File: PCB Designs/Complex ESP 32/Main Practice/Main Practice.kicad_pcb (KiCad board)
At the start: 4 copper layers, 87 parts, among them J1 SS-52400-002, J2 B2B-PH-SM4-TB, J3 GSD090012SEU, J5 Conn_01x04_Pin, J6 Conn_01x05_Pin, Q1 TEMT6000X01, Q2 BC817, Q3 BC817, U1 MCP73871, U2 BME280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

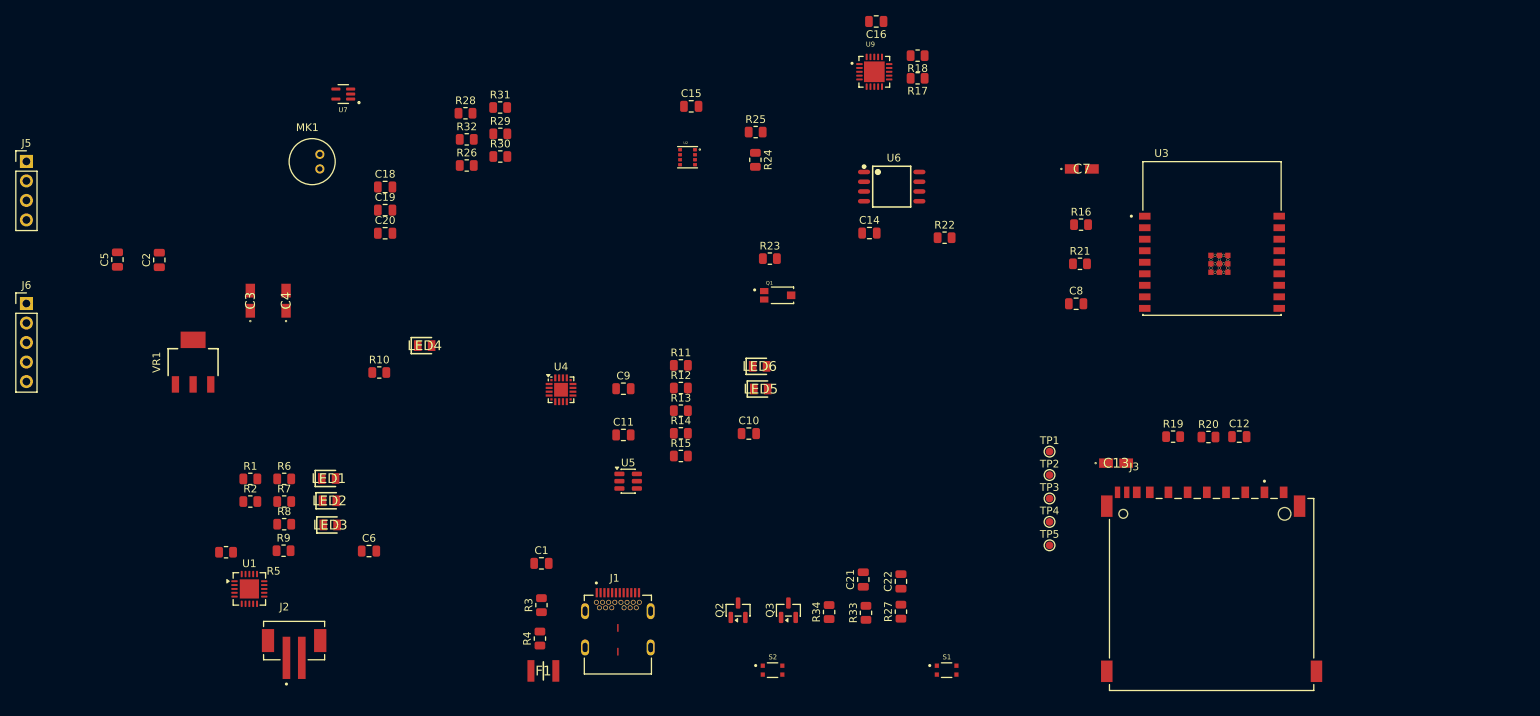
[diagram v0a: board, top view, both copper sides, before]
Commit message: reordered components around for optimal wiring
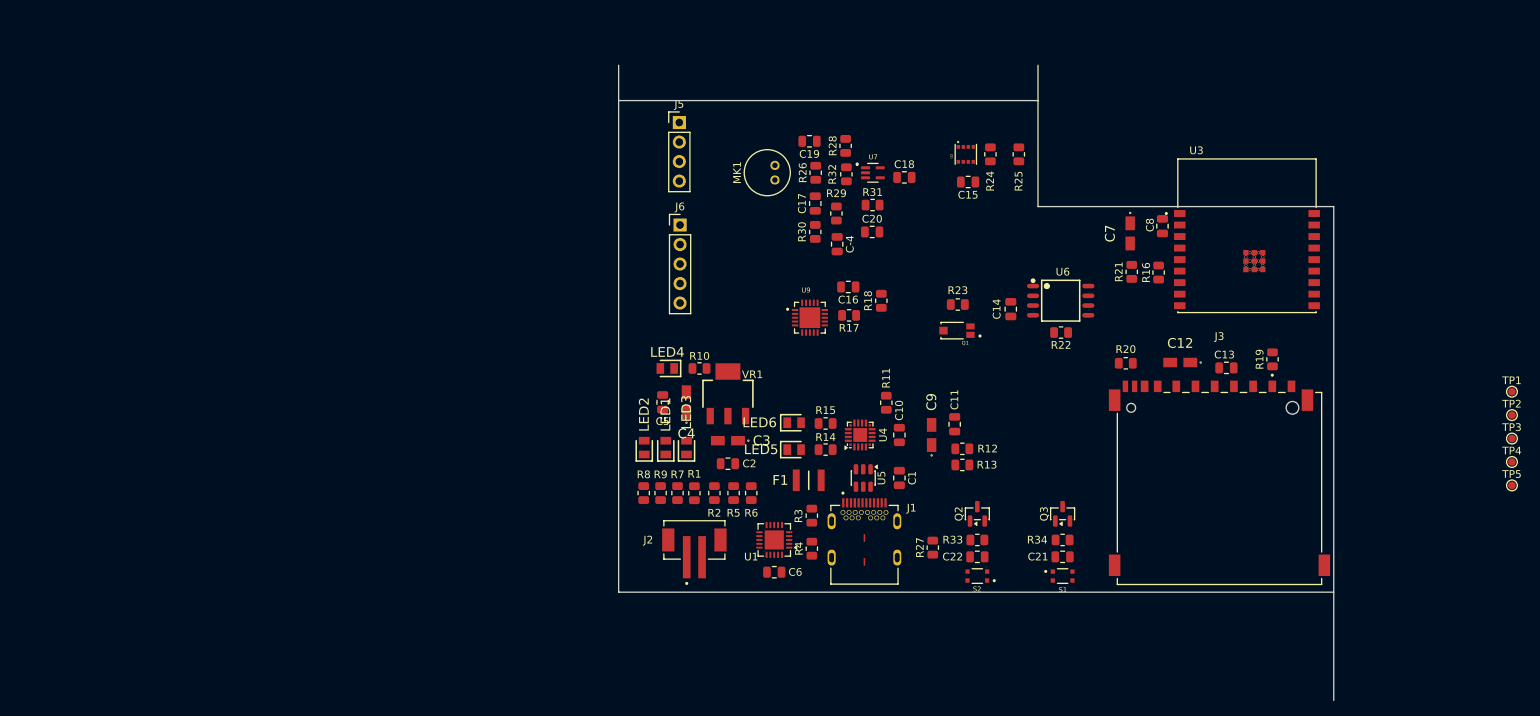
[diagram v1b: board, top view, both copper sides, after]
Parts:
- added C-4: 1u, Capacitor_SMD:C_0805_2012Metric, F.Cu at (179.6, 78.6)
- added C17: 10u, Capacitor_SMD:C_0805_2012Metric, F.Cu at (176.7, 73.3)
- C12: value 0.1u -> 10u; footprint Capacitor_SMD:C_0805_2012Metric -> Footprints:T491A
- C13: value 10u -> 0.1u; footprint Footprints:T491A -> Capacitor_SMD:C_0805_2012Metric
- C9: footprint Capacitor_SMD:C_0805_2012Metric -> Footprints:T491A
- moved J6 85.7 mm to (159.1, 76.1)
- moved J5 85.2 mm to (159.0, 62.8)
- moved C2 78.6 mm to (165.3, 107.2), turned to 0 degrees
- moved C5 73.4 mm to (156.8, 99.2), turned to -90 degrees
- moved VR1 69.7 mm to (165.3, 98.1)
- moved U7 69.7 mm to (184.2, 69.3), turned to 0 degrees
- moved U1 68.6 mm to (171.4, 117.1), turned to 180 degrees
- moved C18 67.6 mm to (188.3, 69.9)
- moved R5 66.5 mm to (166.1, 111.0), turned to 90 degrees
- moved C3 64.8 mm to (165.3, 104.2), turned to 180 degrees
- moved C20 63.4 mm to (184.1, 77.0)
- moved R6 60.8 mm to (168.4, 111.0), turned to 90 degrees
- moved TP1 60.7 mm to (267.4, 97.8)
- moved TP2 60.7 mm to (267.4, 100.8)
- moved TP3 60.7 mm to (267.4, 103.9)
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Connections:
- C20 pad 1: GND -> Net-(U7-IN-)
- MK1 pad OUT: Net-(U7-IN+) -> Net-(C17-Pad1)
- R26 pad 1: Net-(U7-IN+) -> Net-(C17-Pad1)
- R29 pad 1: Net-(U7-IN+) -> Net-(C17-Pad1)
- R30 pad 1: GND -> Net-(U7-IN-)
- R30 pad 2: GND -> Net-(C-4-Pad1)
- R31 pad 1: GND -> Net-(U7-IN-)
- U7 pad 3: GND -> Net-(U7-IN-)
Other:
- board outline added: 93.1 x 82.7 mm
